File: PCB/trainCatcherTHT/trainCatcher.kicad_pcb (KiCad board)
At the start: 2 copper layers, 56 x 48.5 mm, 40 parts, among them J1 Power, J2 break, J3 Conn_01x04_Male, J4 thru, J5 thru, Q1 IRF540N, Q2 IRF540N, U1 MC78L05_TO92, U2 ATtiny13-20PU, U3 SFH617A-1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

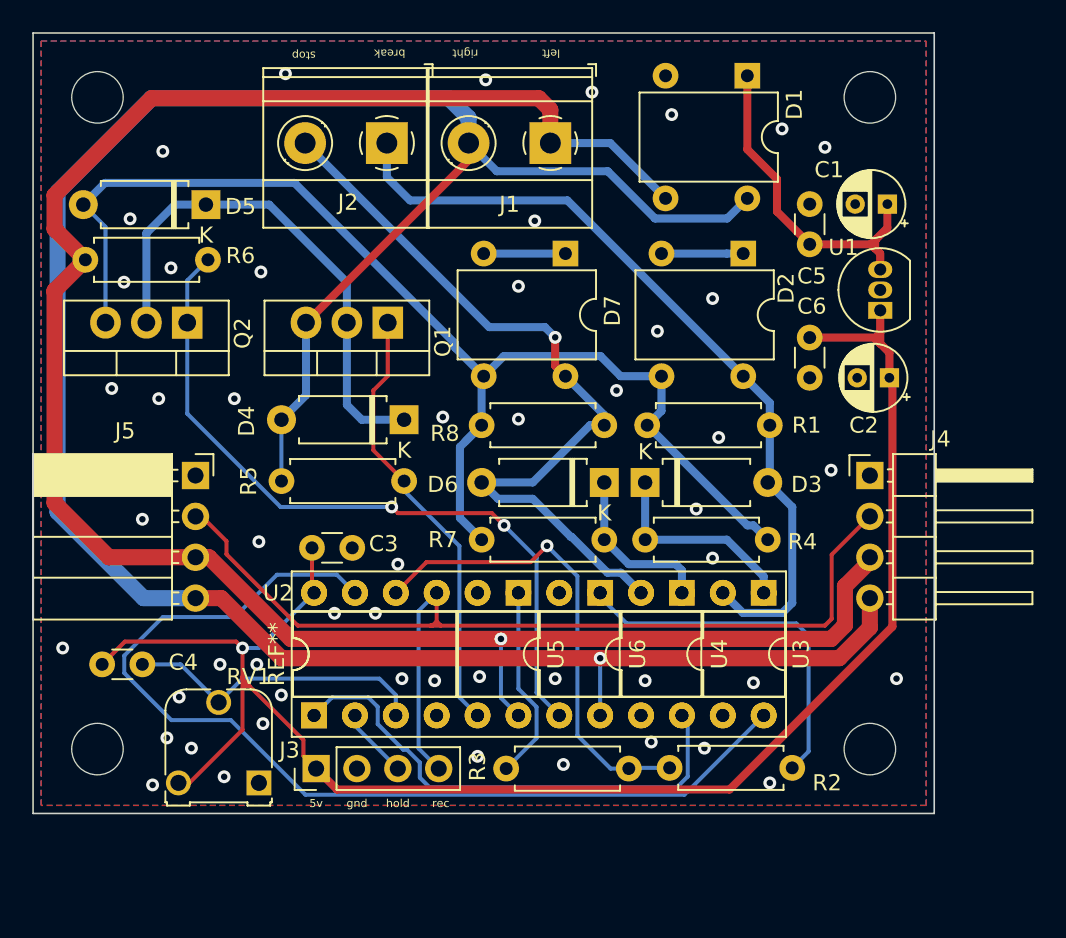
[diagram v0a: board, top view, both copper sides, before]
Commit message: changed PCB design of tht trainCatcher
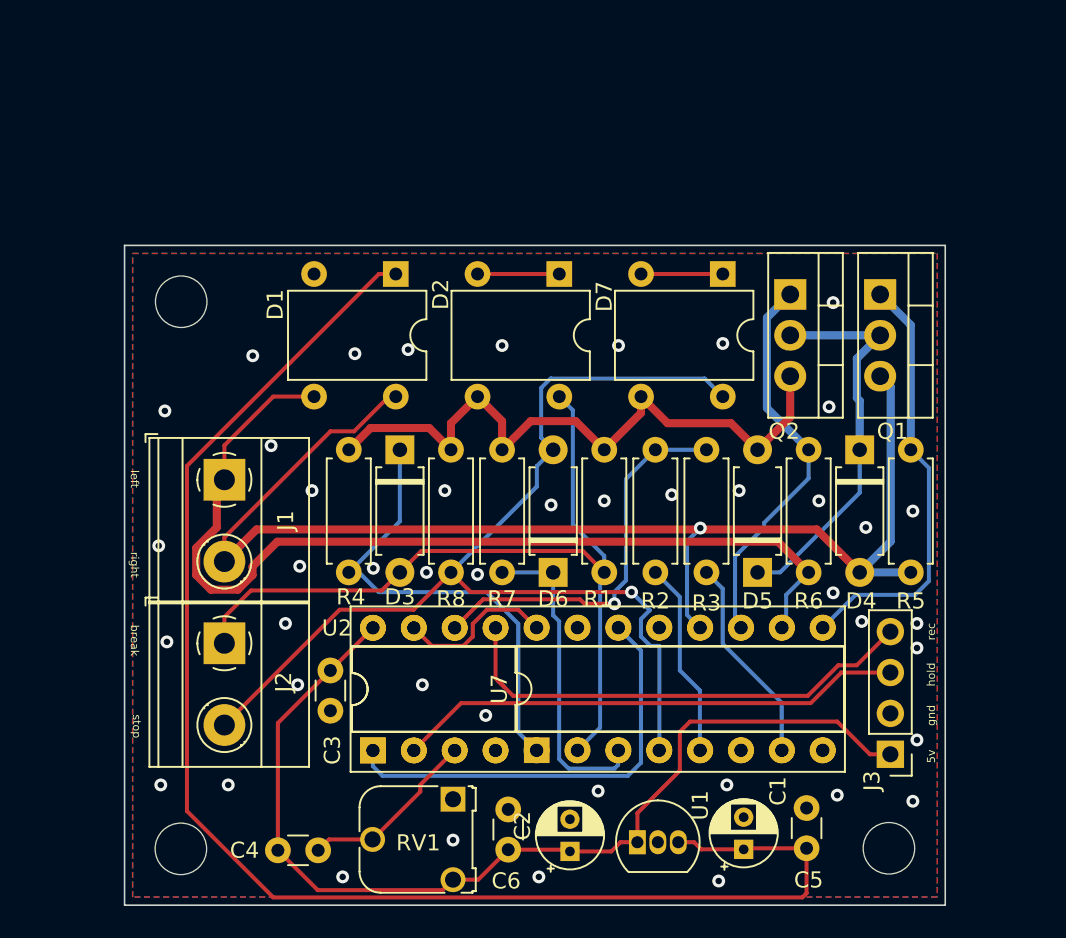
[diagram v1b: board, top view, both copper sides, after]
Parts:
- removed J4: thru, Connector_PinHeader_2.54mm:PinHeader_1x04_P2.54mm_Horizontal
- removed J5: thru, Connector_PinSocket_2.54mm:PinSocket_1x04_P2.54mm_Horizontal
- removed the REF** at (99.3, 46.3)
- removed the REF** at (147.3, 46.3)
- removed U3, U4, U5, U6: SFH617A-1, Package_DIP:DIP-4_W7.62mm
- added REF**: MountingHole_3.2mm_M3, MountingHole:MountingHole_3.2mm_M3, F.Cu at (104.5, 59.0)
- added U7: LTV-847, Package_DIP:DIP-16_W7.62mm, F.Cu at (126.6, 86.9)
- moved D5 41.2 mm to (140.3, 75.8), turned to 90 degrees
- moved C1 41.1 mm to (139.5, 93.0), turned to 90 degrees
- moved R5 39.5 mm to (149.9, 75.8), turned to 90 degrees
- moved R6 39.1 mm to (143.5, 68.2), turned to 270 degrees
- moved C5 37.5 mm to (143.4, 90.5)
- moved Q2 37.5 mm to (142.4, 58.5), turned to 270 degrees
- moved U1 36.3 mm to (132.9, 92.6), turned to 0 degrees
- moved J3 35.7 mm to (148.6, 87.1), turned to 180 degrees
- moved C2 35.5 mm to (128.7, 93.2), turned to 90 degrees
- moved C6 32.7 mm to (124.8, 90.6), turned to 270 degrees
- moved J2 32.7 mm to (107.2, 80.2), turned to 270 degrees
- moved Q1 30.6 mm to (148.0, 58.5), turned to 270 degrees
- moved J1 29.1 mm to (107.2, 70.1), turned to 270 degrees
- moved D4 28.4 mm to (146.7, 68.2), turned to 270 degrees
- moved D1 25.1 mm to (117.9, 57.3)
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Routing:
- net /rightTrack: track 155.6 -> 80.5 mm
- net Net-(C1-Pad1): track 21.2 -> 91.2 mm
- net /leftTrack: track 128.0 -> 60.5 mm, vias 1 -> 0
- net /break: track 62.9 -> 9.95 mm
- net +5V: track 102.2 -> 63.1 mm, vias 1 -> 0
- net Net-(D2-Pad3): track 77.7 -> 41.5 mm
- net /rec: track 64.5 -> 30.3 mm
- net /hold: track 4.41 -> 31.6 mm
- net Net-(Q2-Pad1): track 45.9 -> 24.4 mm, vias 2 -> 0
- net /stopTrack: track 49.1 -> 67.5 mm
- net Net-(D3-Pad1): track 12.9 -> 29.1 mm
- net Net-(R2-Pad1): track 22.8 -> 12.2 mm
- net Net-(D6-Pad1): track 10.6 -> 19.8 mm, vias 0 -> 1
- net Net-(D4-Pad1): track 32.3 -> 24.4 mm
- net /breakSpeed: track 19.0 -> 11.3 mm
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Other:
- board size 56 x 48.5 mm -> 51 x 41 mm

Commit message: Fixed the PCB to contain the buffer section as well. Also the right rail should now be switched and sensed well. The program has been succesfully altered to issue a 30s unconditional stop if the gold line and signal line are tied togather. This allows the traincatcher to be used on a pass-throug station without an extra relay or something
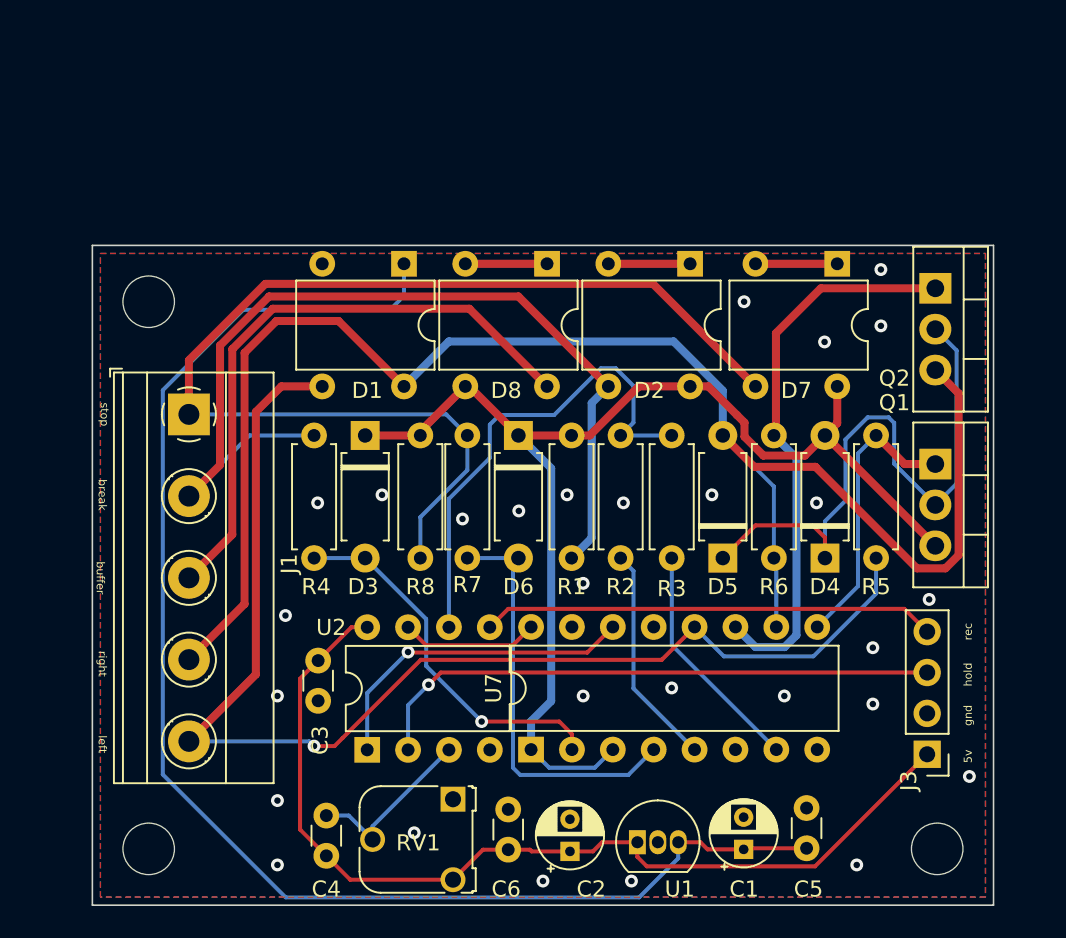
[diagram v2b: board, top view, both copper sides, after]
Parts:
- removed J2: break, TerminalBlock_Phoenix:TerminalBlock_Phoenix_MKDS-1,5-2-5.08_1x02_P5.08mm_Horizontal
- removed the REF** at (116.4, 86.9)
- added D8: D, Diode_THT:Diode_Bridge_DIP-4_W7.62mm_P5.08mm, F.Cu at (127.3, 56.6)
- J1: value Power -> break; footprint TerminalBlock_Phoenix:TerminalBlock_Phoenix_MKDS-1,5-2-5.08_1x02_P5.08mm_Horizontal -> TerminalBlock_Phoenix:TerminalBlock_Phoenix_MKDS-1,5-5-5.08_1x05_P5.08mm_Horizontal
- moved Q1 11.1 mm to (151.4, 69.1)
- moved Q2 9.03 mm to (151.4, 58.2)
- moved D6 8.78 mm to (125.5, 67.3), turned to -90 degrees
- moved D2 8.15 mm to (136.1, 56.6)
- moved D7 7.14 mm to (145.3, 56.6)
- moved D4 7.07 mm to (144.5, 74.9), turned to 90 degrees
- moved R1 7.03 mm to (128.8, 74.9), turned to 90 degrees
- moved R8 7.00 mm to (119.4, 74.9), turned to 90 degrees
- moved J1 4.62 mm to (105.0, 66.0)
- moved REF** 3.00 mm to (151.5, 93.0)
- moved D5 2.33 mm to (138.2, 74.9)
- moved R2 2.33 mm to (131.8, 74.9)
- moved R5 2.33 mm to (147.7, 74.9)
- moved D3 2.33 mm to (116.0, 67.3)
- moved R4 2.33 mm to (112.8, 74.9)
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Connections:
- D1 pad 3: /leftTrack -> /leftMain
- D1 pad 4: /rightTrack -> /rightMain
- D2 pad 3: Net-(D2-Pad3) -> /breakSection
- D2 pad 4: /breakSection -> Net-(D2-Pad4)
- D3 pad 1: Net-(D3-Pad1) -> Net-(D2-Pad4)
- D3 pad 2: /breakSection -> Net-(R4-Pad1)
- D4 pad 2: /rightTrack -> Net-(D2-Pad4)
- D5 pad 2: Net-(D2-Pad3) -> /rightMain
- D6 pad 1: Net-(D6-Pad1) -> Net-(D2-Pad4)
- D6 pad 2: /stopTrack -> Net-(R7-Pad1)
- D7 pad 3: Net-(D2-Pad3) -> /stopTrack
- D7 pad 4: /stopTrack -> Net-(D2-Pad4)
- J1 pad 1: /leftTrack -> /stopTrack
- J1 pad 2: /rightTrack -> /breakSection
- Q1 pad 3: /rightTrack -> Net-(D2-Pad4)
- Q2 pad 3: Net-(D2-Pad3) -> /rightMain
- R1 pad 1: Net-(D2-Pad3) -> /breakSection
- R1 pad 2: /breakSection -> Net-(D2-Pad4)
- R4 pad 1: Net-(D3-Pad1) -> Net-(R4-Pad1)
- R4 pad 2: Net-(D2-Pad3) -> /breakSection
- R5 pad 1: /rightTrack -> /leftMain
- R6 pad 2: /leftTrack -> /rightMain
- R7 pad 1: Net-(D6-Pad1) -> Net-(R7-Pad1)
- R7 pad 2: Net-(D2-Pad3) -> /stopTrack
- R8 pad 1: Net-(D2-Pad3) -> /stopTrack
- R8 pad 2: /stopTrack -> Net-(D2-Pad4)
- U7 pad 1: Net-(D3-Pad1) -> Net-(D2-Pad4)
- U7 pad 10: /leftTrack -> /rightMain
- U7 pad 12: /rightTrack -> /leftMain
- U7 pad 2: /breakSection -> Net-(R4-Pad1)
- U7 pad 3: Net-(D6-Pad1) -> Net-(D2-Pad4)
- U7 pad 4: /stopTrack -> Net-(R7-Pad1)
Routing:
- net /rightMain: track 0.00 -> 101.7 mm
- net /rightTrack: track 80.5 -> 0.00 mm, vias 1 -> 0
- net /leftMain: track 0.00 -> 77.4 mm, vias 0 -> 1
- net Net-(D2-Pad4): track 0.00 -> 75.3 mm
- net /leftTrack: track 60.5 -> 0.00 mm
- net Net-(D2-Pad3): track 41.5 -> 0.00 mm
- net /bufferSection: track 0.00 -> 38.2 mm
- net Net-(D3-Pad1): track 29.1 -> 0.00 mm
- net Net-(R7-Pad1): track 0.00 -> 25.9 mm
- net Net-(R4-Pad1): track 0.00 -> 23.2 mm, vias 0 -> 1
- net Net-(D6-Pad1): track 19.8 -> 0.00 mm, vias 1 -> 0
- net Net-(D4-Pad1): track 24.4 -> 38.6 mm
- net Net-(Q2-Pad1): track 24.4 -> 35.1 mm
- net Net-(Q1-Pad1): track 26.9 -> 17.8 mm
- net /breakSection: track 51.3 -> 58.8 mm
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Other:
- board size 51 x 41 mm -> 56 x 41 mm
- net class Default removed
- board text added: "buffer"
